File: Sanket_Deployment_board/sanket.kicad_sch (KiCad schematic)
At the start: 42 parts, among them J2 Conn_02x03_Counter_Clockwise, J3 Conn_02x03_Counter_Clockwise, U1 SN74LVC1G17QDCKRQ1

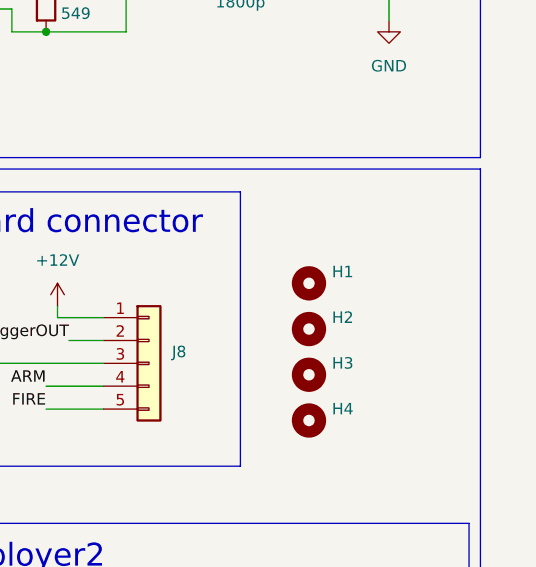
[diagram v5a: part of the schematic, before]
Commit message: Replace a mounting hole to mounting pad to ground
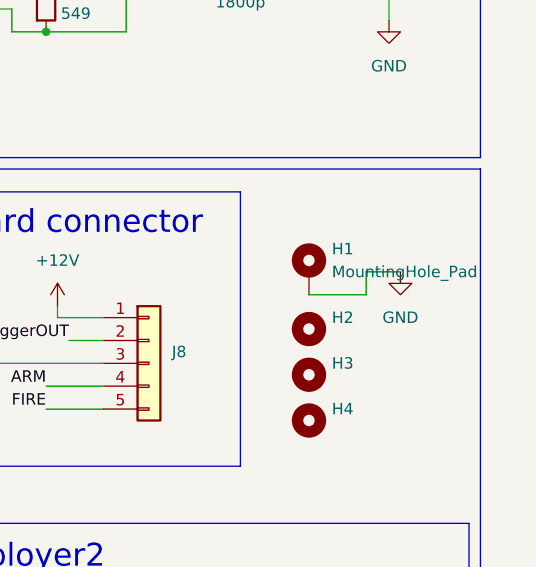
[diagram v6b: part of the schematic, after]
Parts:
- removed H1: (no value), MountingHole:MountingHole_3.2mm_M3, symbol Mechanical:MountingHole
- added H1: MountingHole_Pad, MountingHole:MountingHole_3.2mm_M3_Pad, symbol Mechanical:MountingHole_Pad
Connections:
- net GND: now also H1.1
